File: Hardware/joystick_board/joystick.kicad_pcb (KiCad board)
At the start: 2 copper layers, 80.8 x 60.1 mm, 18 parts, among them J1 Conn_01x40, J2 DE9_Socket_MountingHoles, J3 DE9_Socket_MountingHoles, U1 74HC00, U2 74HC245, U3 74HC245

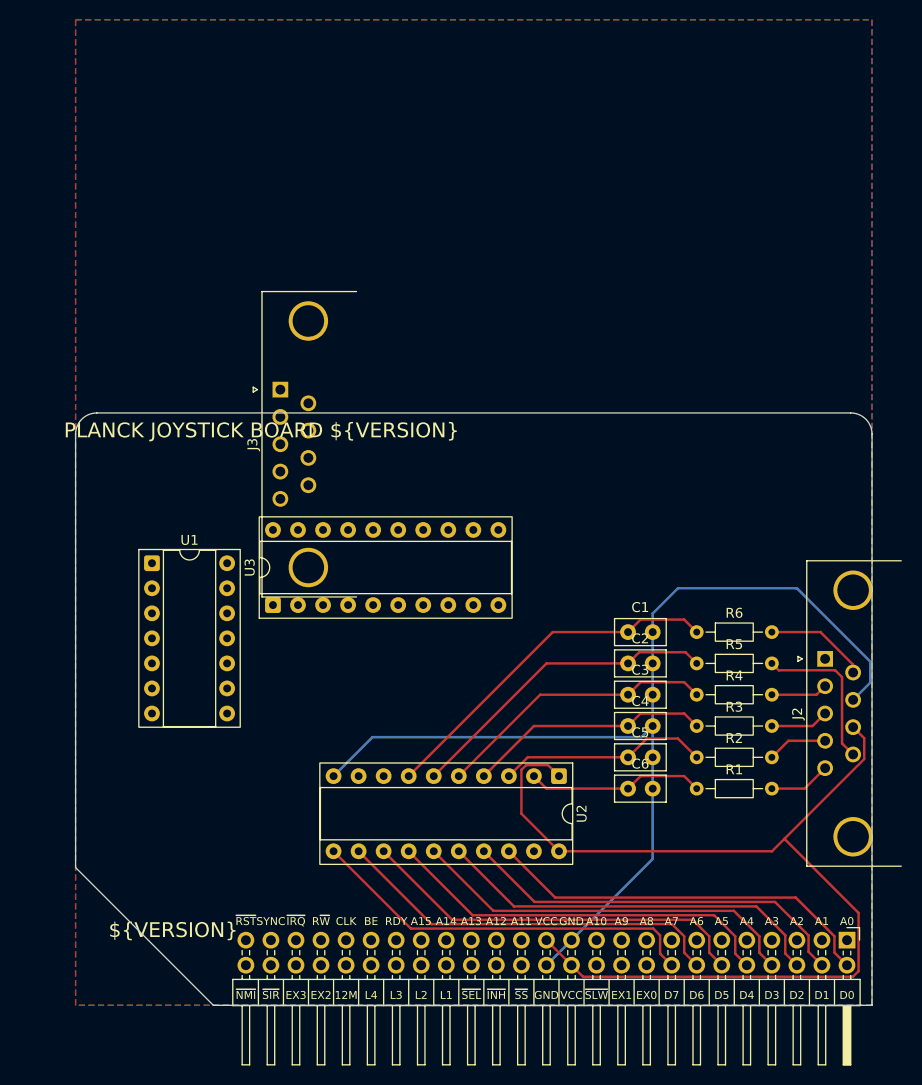
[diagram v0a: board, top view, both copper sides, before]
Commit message: some work on joystick pcb, should have all parts now, but joystick port footprints are still to be done
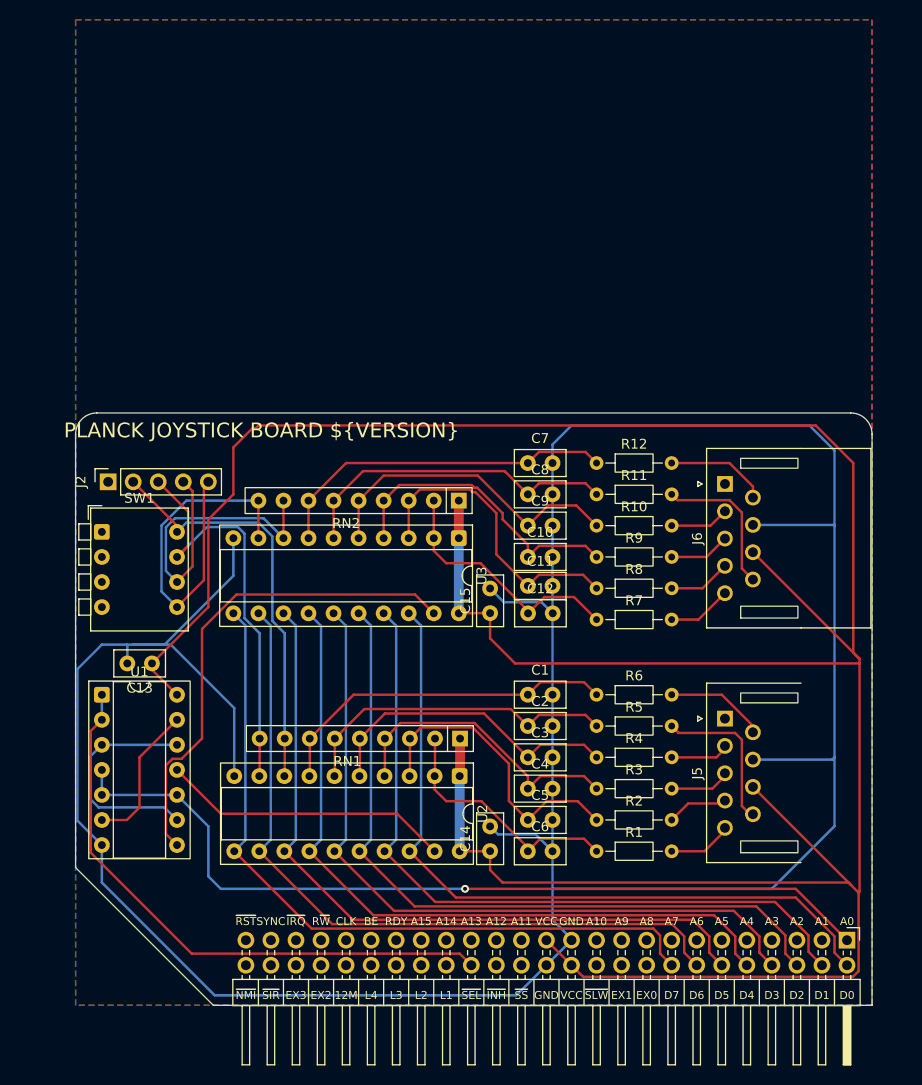
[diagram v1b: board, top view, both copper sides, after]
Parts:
- removed J3: DE9_Socket_MountingHoles, Connector_Dsub:DSUB-9_Socket_Horizontal_P2.77x2.84mm_EdgePinOffset4.94mm_Housed_MountingHolesOffset4.94mm
- added C10: C, Capacitor_THT:C_Disc_D5.0mm_W2.5mm_P2.50mm, F.Cu at (151.2, 92.1)
- added C11: C, Capacitor_THT:C_Disc_D5.0mm_W2.5mm_P2.50mm, F.Cu at (151.2, 95.0)
- added C12: C, Capacitor_THT:C_Disc_D5.0mm_W2.5mm_P2.50mm, F.Cu at (151.2, 97.8)
- added C13: C, Capacitor_THT:C_Disc_D5.0mm_W2.5mm_P2.50mm, F.Cu at (113.0, 102.9)
- added C14: C, Capacitor_THT:C_Disc_D5.0mm_W2.5mm_P2.50mm, F.Cu at (147.3, 121.9)
- added C15: C, Capacitor_THT:C_Disc_D5.0mm_W2.5mm_P2.50mm, F.Cu at (147.3, 97.8)
- added C7: C, Capacitor_THT:C_Disc_D5.0mm_W2.5mm_P2.50mm, F.Cu at (151.2, 82.5)
- added C8: C, Capacitor_THT:C_Disc_D5.0mm_W2.5mm_P2.50mm, F.Cu at (151.2, 85.7)
- added C9: C, Capacitor_THT:C_Disc_D5.0mm_W2.5mm_P2.50mm, F.Cu at (151.2, 88.9)
- added J5: Sega_DE9_joystick_connector, Library:Sega DE9 joystick connector, F.Cu at (171.1, 108.5)
- added J6: Sega_DE9_joystick_connector, Library:Sega DE9 joystick connector, F.Cu at (171.1, 84.7)
- added R10: R, Resistor_THT:R_Axial_DIN0204_L3.6mm_D1.6mm_P7.62mm_Horizontal, F.Cu at (158.1, 88.9)
- added R11: R, Resistor_THT:R_Axial_DIN0204_L3.6mm_D1.6mm_P7.62mm_Horizontal, F.Cu at (158.1, 85.7)
- added R12: R, Resistor_THT:R_Axial_DIN0204_L3.6mm_D1.6mm_P7.62mm_Horizontal, F.Cu at (158.1, 82.5)
- added R7: R, Resistor_THT:R_Axial_DIN0204_L3.6mm_D1.6mm_P7.62mm_Horizontal, F.Cu at (158.1, 98.4)
- added R8: R, Resistor_THT:R_Axial_DIN0204_L3.6mm_D1.6mm_P7.62mm_Horizontal, F.Cu at (158.1, 95.2)
- added R9: R, Resistor_THT:R_Axial_DIN0204_L3.6mm_D1.6mm_P7.62mm_Horizontal, F.Cu at (158.1, 92.1)
- added RN1: R_Network08, Resistor_THT:R_Array_SIP9, F.Cu at (144.3, 110.5)
- added RN2: R_Network08, Resistor_THT:R_Array_SIP9, F.Cu at (144.1, 86.4)
- added SW1: SW_DIP_x04, Button_Switch_THT:SW_DIP_SPSTx04_Piano_CTS_Series194-4MSTN_W7.62mm_P2.54mm, F.Cu at (108.0, 89.5)
- J2: value DE9_Socket_MountingHoles -> Conn_01x05_Pin; footprint Connector_Dsub:DSUB-9_Socket_Horizontal_P2.77x2.84mm_EdgePinOffset4.94mm_Housed_MountingHolesOffset4.94mm -> Connector_PinSocket_2.54mm:PinSocket_1x05_P2.54mm_Vertical
- moved J2 74.9 mm to (108.6, 84.5)
- moved U3 20.0 mm to (144.1, 90.2), turned to -90 degrees
- moved U1 14.3 mm to (108.0, 106.0)
- moved C1 12.0 mm to (151.2, 106.0)
- moved C5 12.0 mm to (151.2, 118.7)
- moved C6 12.0 mm to (151.2, 121.9)
- moved R1 12.0 mm to (158.1, 121.9)
- moved R2 12.0 mm to (158.1, 118.7)
- moved R6 12.0 mm to (158.1, 106.0)
- moved C2 12.0 mm to (151.2, 109.2)
- moved C3 12.0 mm to (151.2, 112.4)
- moved C4 12.0 mm to (151.2, 115.6)
- moved R3 12.0 mm to (158.1, 115.6)
- moved R4 12.0 mm to (158.1, 112.4)
- moved R5 12.0 mm to (158.1, 109.2)
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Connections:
- J2 pad 1: unconnected-(J2-Pad1) -> GND
- J2 pad 2: Net-(J2-Pad2) -> ~{USR1}
- J2 pad 3: Net-(J2-Pad3) -> ~{USR2}
- J2 pad 4: Net-(J2-Pad4) -> ~{USR3}
- J2 pad 5: Net-(J2-Pad5) -> ~{USR4}
- R1 pad 2: Net-(J2-Pad5) -> Net-(J5-Pad5)
- R2 pad 2: Net-(J2-Pad4) -> Net-(J5-Pad4)
- R3 pad 2: Net-(J2-Pad3) -> Net-(J5-Pad3)
- R4 pad 2: Net-(J2-Pad2) -> Net-(J5-Pad2)
- R5 pad 2: Net-(J2-Pad9) -> Net-(J5-Pad9)
- R6 pad 2: Net-(J2-Pad6) -> Net-(J5-Pad6)
- U1 pad 1: unconnected-(U1-Pad1) -> ~{SLOT_SEL}
- U1 pad 10: unconnected-(U1-Pad10) -> A0
- U1 pad 11: unconnected-(U1-Pad11) -> ~{SEL_JOY1}
- U1 pad 12: unconnected-(U1-Pad12) -> Net-(U1-Pad12)
- U1 pad 13: unconnected-(U1-Pad13) -> Net-(U1-Pad13)
- U1 pad 14: unconnected-(U1E-VCC-Pad14) -> +5V
- U1 pad 2: unconnected-(U1-Pad2) -> ~{SLOT_SEL}
- U1 pad 3: unconnected-(U1-Pad3) -> Net-(U1-Pad12)
- U1 pad 4: unconnected-(U1-Pad4) -> A0
- U1 pad 5: unconnected-(U1-Pad5) -> A0
- U1 pad 6: unconnected-(U1-Pad6) -> Net-(U1-Pad13)
- U1 pad 7: unconnected-(U1E-GND-Pad7) -> GND
- U1 pad 8: unconnected-(U1-Pad8) -> ~{SEL_JOY2}
- U1 pad 9: unconnected-(U1-Pad9) -> Net-(U1-Pad12)
- U2 pad 19: unconnected-(U2-CE-Pad19) -> ~{SEL_JOY1}
- U2 pad 8: unconnected-(U2-A6-Pad8) -> ~{USR1}
- U2 pad 9: unconnected-(U2-A7-Pad9) -> ~{USR2}
- U3 pad 1: unconnected-(U3-A->B-Pad1) -> +5V
- U3 pad 10: unconnected-(U3-GND-Pad10) -> GND
- U3 pad 11: unconnected-(U3-B7-Pad11) -> D7
- U3 pad 12: unconnected-(U3-B6-Pad12) -> D6
- U3 pad 13: unconnected-(U3-B5-Pad13) -> D5
- U3 pad 14: unconnected-(U3-B4-Pad14) -> D4
- U3 pad 15: unconnected-(U3-B3-Pad15) -> D3
- U3 pad 16: unconnected-(U3-B2-Pad16) -> D2
- U3 pad 17: unconnected-(U3-B1-Pad17) -> D1
- U3 pad 18: unconnected-(U3-B0-Pad18) -> D0
- U3 pad 19: unconnected-(U3-CE-Pad19) -> ~{SEL_JOY2}
- U3 pad 2: unconnected-(U3-A0-Pad2) -> Net-(RN2-R1)
- U3 pad 20: unconnected-(U3-VCC-Pad20) -> +5V
- U3 pad 3: unconnected-(U3-A1-Pad3) -> Net-(RN2-R2)
- U3 pad 4: unconnected-(U3-A2-Pad4) -> Net-(RN2-R3)
- U3 pad 5: unconnected-(U3-A3-Pad5) -> Net-(RN2-R4)
- U3 pad 6: unconnected-(U3-A4-Pad6) -> Net-(RN2-R5)
- U3 pad 7: unconnected-(U3-A5-Pad7) -> Net-(RN2-R6)
- U3 pad 8: unconnected-(U3-A6-Pad8) -> ~{USR3}
- U3 pad 9: unconnected-(U3-A7-Pad9) -> ~{USR4}
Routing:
- net +5V: track 102.8 -> 319.9 mm
- net GND: track 105.4 -> 305.0 mm
- net A0: track 0.00 -> 87.2 mm, vias 0 -> 1
- net ~{SLOT_SEL}: track 0.00 -> 59.8 mm
- net ~{SEL_JOY2}: track 0.00 -> 50.8 mm
- net ~{USR2}: track 0.00 -> 43.0 mm
- net ~{USR1}: track 0.00 -> 42.4 mm
- net ~{USR4}: track 0.00 -> 37.6 mm
- net Net-(RN2-R6): track 0.00 -> 35.5 mm
- net D5: track 40.1 -> 75.6 mm
- net D4: track 40.1 -> 75.3 mm
- net D1: track 40.1 -> 75.3 mm
- net D6: track 40.1 -> 75.3 mm
- net D0: track 40.1 -> 75.3 mm
- net D3: track 40.1 -> 75.3 mm
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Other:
- board text removed: "${VERSION}"
